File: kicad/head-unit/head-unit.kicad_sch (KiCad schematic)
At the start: 59 parts, among them J1 Debug_Port, J2 Relay_Main_Power, J3 Steering_Wheel, J4 Power Port, J5 Car Connection, J6 Relay_Ign_Detect, J7 Pi, J8 DAC+, K1 Relay_Aux_Power, K2 Relay_Amplifier, SW1 SW_RST, U1 ADP1108AN-3.3, U2 STM32F401RCTx, U3 ADP1108AN-5

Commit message: Dankje Douwe
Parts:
- removed C10: 100uF, Capacitor_SMD:C_1206_3216Metric, symbol Device:C
- removed L2: 20nH, Inductor_SMD:L_0603_1608Metric, symbol Device:L
- removed R5: 100R, Resistor_SMD:R_0402_1005Metric, symbol Device:R
- removed R6: 456K, Resistor_SMD:R_0402_1005Metric, symbol Device:R
- removed R7: 33K, Resistor_SMD:R_0402_1005Metric, symbol Device:R
- removed U3: ADP1108AN-5, Package_DIP:DIP-8_W7.62mm, symbol Regulator_Switching:ADP1108AN-5
- added C12: 100uF, Capacitor_SMD:C_1206_3216Metric, symbol Device:C
- added J9: Amp_Remote, symbol Connector_Generic:Conn_01x01
- R3: value 456K -> 9K
- R4: value 33K -> 3K3
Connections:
- net +5V: now also D2.1 (K), K1.A2
- net Aux_Power: no longer K1.A2
- net GND: now also C12.2
- net +12V_Switched: now reaches J2.87, K1.14, R1.1, U1.2 (Vin), U1.3 (SW1)
- net +12V_Switched: now also C12.1
- net Amp_Remote: no longer names the net of K2.14
- net Amp_Remote: now also J9.1 (Pin_1)
- no-connect marks 66 -> 64
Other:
- added sheet 12 to 5V (12v_to_5v.kicad_sch)
- moved on the sheet: J2, J6

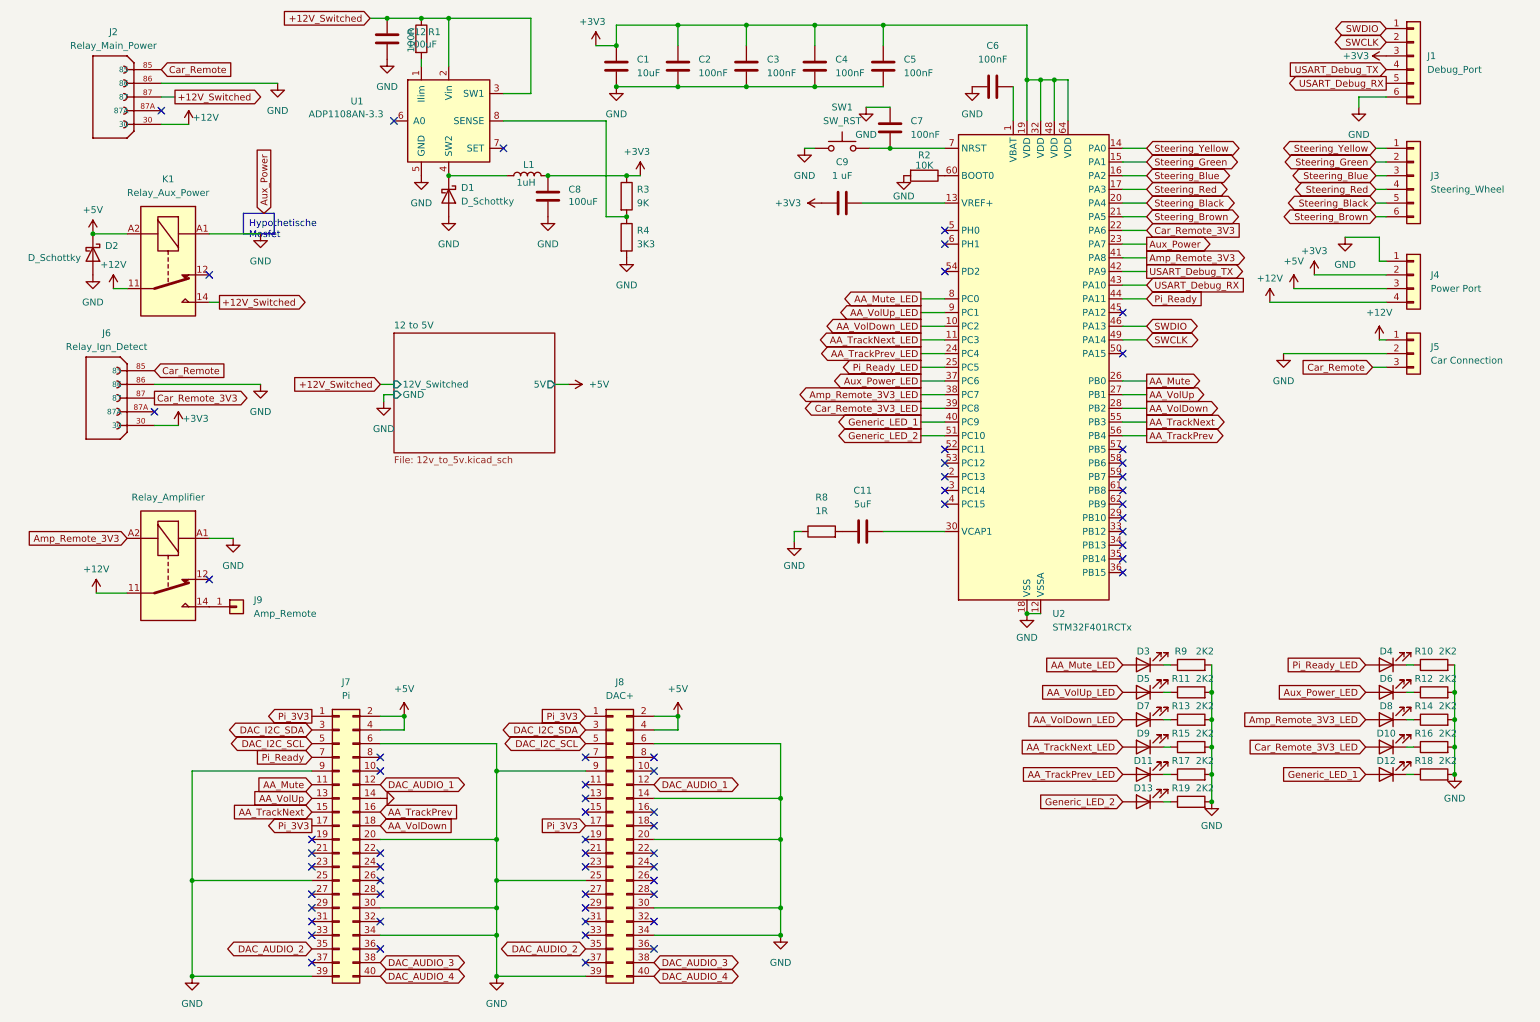
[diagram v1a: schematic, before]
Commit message: Fix mosfets, switch to screw terminals and XT60
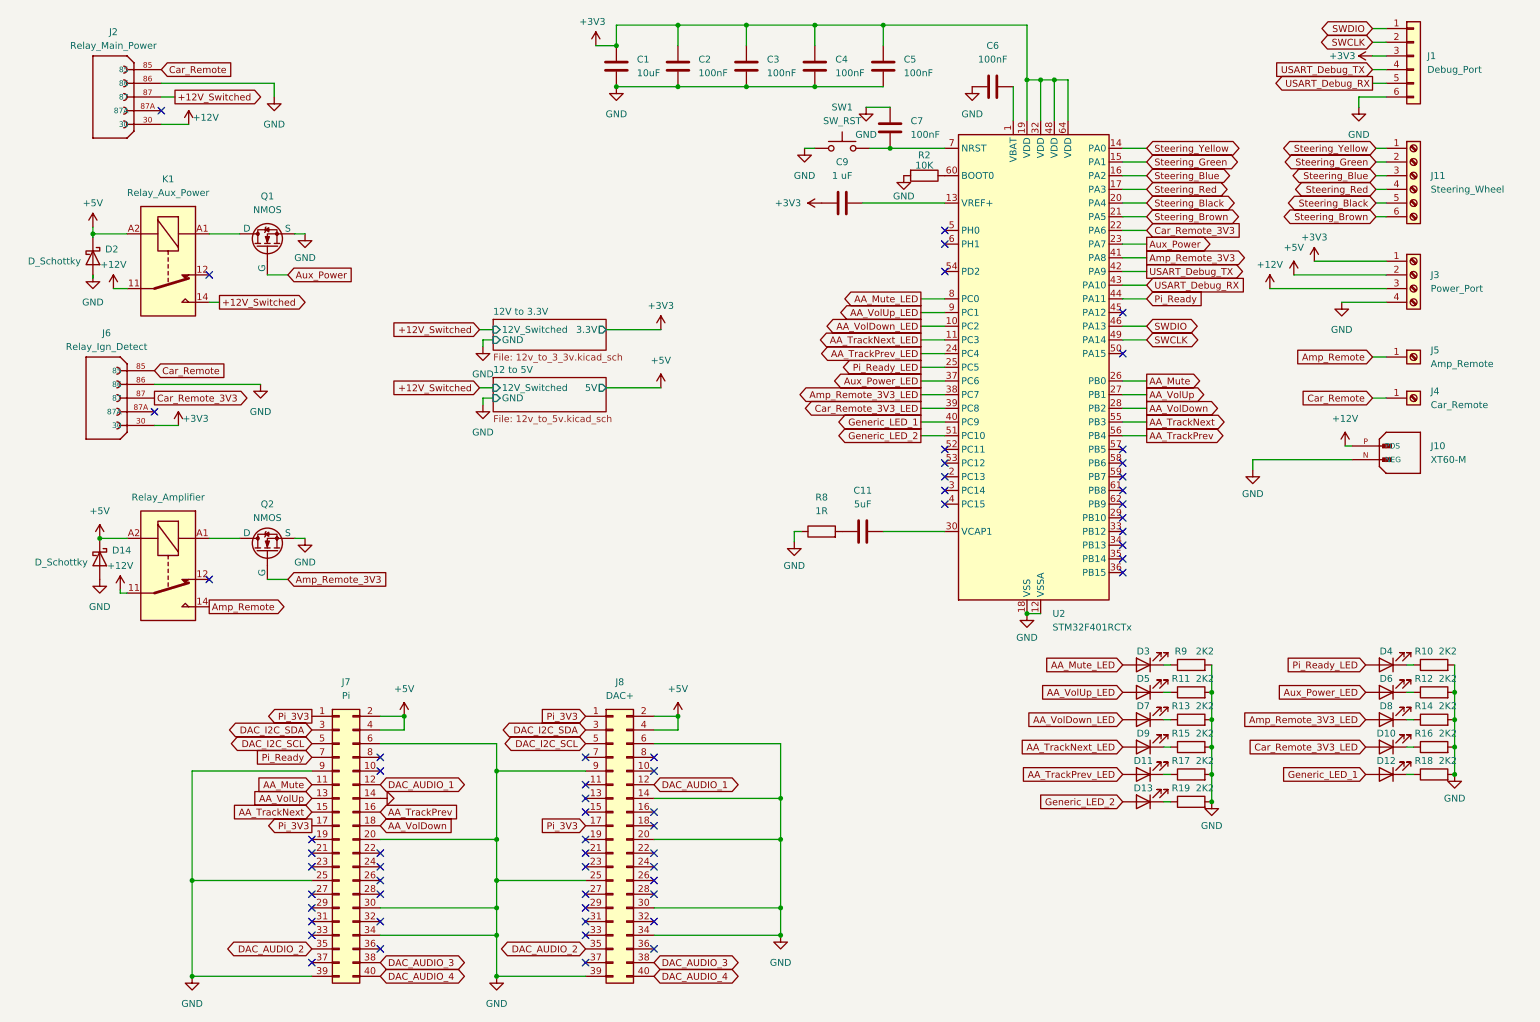
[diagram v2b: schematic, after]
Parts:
- removed C12, C8: 100uF, Capacitor_SMD:C_1206_3216Metric, symbol Device:C
- removed D1: D_Schottky, Diode_SMD:D_0603_1608Metric, symbol Device:D_Schottky
- removed J3: Steering_Wheel, Connector_PinHeader_2.54mm:PinHeader_1x06_P2.54mm_Vertical, symbol Connector_Generic:Conn_01x06
- removed J4: Power Port, Connector_PinHeader_2.54mm:PinHeader_1x04_P2.54mm_Vertical, symbol Connector_Generic:Conn_01x04
- removed J5: Car Connection, Connector_PinHeader_2.54mm:PinHeader_1x03_P2.54mm_Vertical, symbol Connector_Generic:Conn_01x03
- removed J9: Amp_Remote, symbol Connector_Generic:Conn_01x01
- removed L1: 1uH, Inductor_SMD:L_0402_1005Metric, symbol Device:L
- removed R1: 100R, Resistor_SMD:R_0402_1005Metric, symbol Device:R
- removed R3: 9K, Resistor_SMD:R_0402_1005Metric, symbol Device:R
- removed R4: 3K3, Resistor_SMD:R_0402_1005Metric, symbol Device:R
- removed U1: ADP1108AN-3.3, Package_DIP:DIP-8_W7.62mm, symbol Regulator_Switching:ADP1108AN-3.3
- added D14: D_Schottky, Diode_SMD:D_0603_1608Metric, symbol Device:D_Schottky
- added J10: XT60-M, xt60:AMASS_XT60-M, symbol XT60-M:XT60-M
- added J11: Steering_Wheel, TerminalBlock:TerminalBlock_bornier-6_P5.08mm, symbol Connector:Screw_Terminal_01x06
- added J3: Power_Port, TerminalBlock:TerminalBlock_bornier-4_P5.08mm, symbol Connector:Screw_Terminal_01x04
- added J4: Car_Remote, TerminalBlock_MetzConnect:TerminalBlock_MetzConnect_360272_1x01_Horizontal_ScrewM2.6, symbol Connector:Screw_Terminal_01x01
- added J5: Amp_Remote, TerminalBlock_MetzConnect:TerminalBlock_MetzConnect_360272_1x01_Horizontal_ScrewM2.6, symbol Connector:Screw_Terminal_01x01
- added Q1, Q2: NMOS, Button_Switch_SMD:SW_SPDT_CK-JS102011SAQN, symbol Simulation_SPICE:NMOS
- J2, J6: footprint external_symbols:TE_VCF4-1000 -> vcf4:TE_VCF4-1000
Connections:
- net +12V: now also J10.P (POS), J3.3 (Pin_3)
- net +3V3: now also J3.1 (Pin_1)
- net +5V: now also K2.A2, D14.1 (K), J3.2 (Pin_2)
- net Amp_Remote_3V3: now also Q2.2 (G); no longer K2.A2
- net Aux_Power: now also Q1.2 (G)
- net Car_Remote: now also J4.1 (Pin_1)
- net GND: now also D14.2 (A), J10.N (NEG), J3.4 (Pin_4), Q1.3 (S), Q2.3 (S); no longer K1.A1, K2.A1
- net Steering_Black: now also J11.5 (Pin_5)
- net Steering_Blue: now also J11.3 (Pin_3)
- net Steering_Brown: now also J11.6 (Pin_6)
- net Steering_Green: now also J11.2 (Pin_2)
- net Steering_Red: now also J11.4 (Pin_4)
- net Steering_Yellow: now also J11.1 (Pin_1)
- net Amp_Remote: now reaches K2.14
- net Amp_Remote: now also J5.1 (Pin_1)
- new net: K2.A1, Q2.1 (D)
- new net: K1.A1, Q1.1 (D)
- no-connect marks 64 -> 62
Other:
- added sheet 12V to 3.3V (12v_to_3_3v.kicad_sch)
- moved on the sheet: D2

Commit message: Add I2C, begin routing
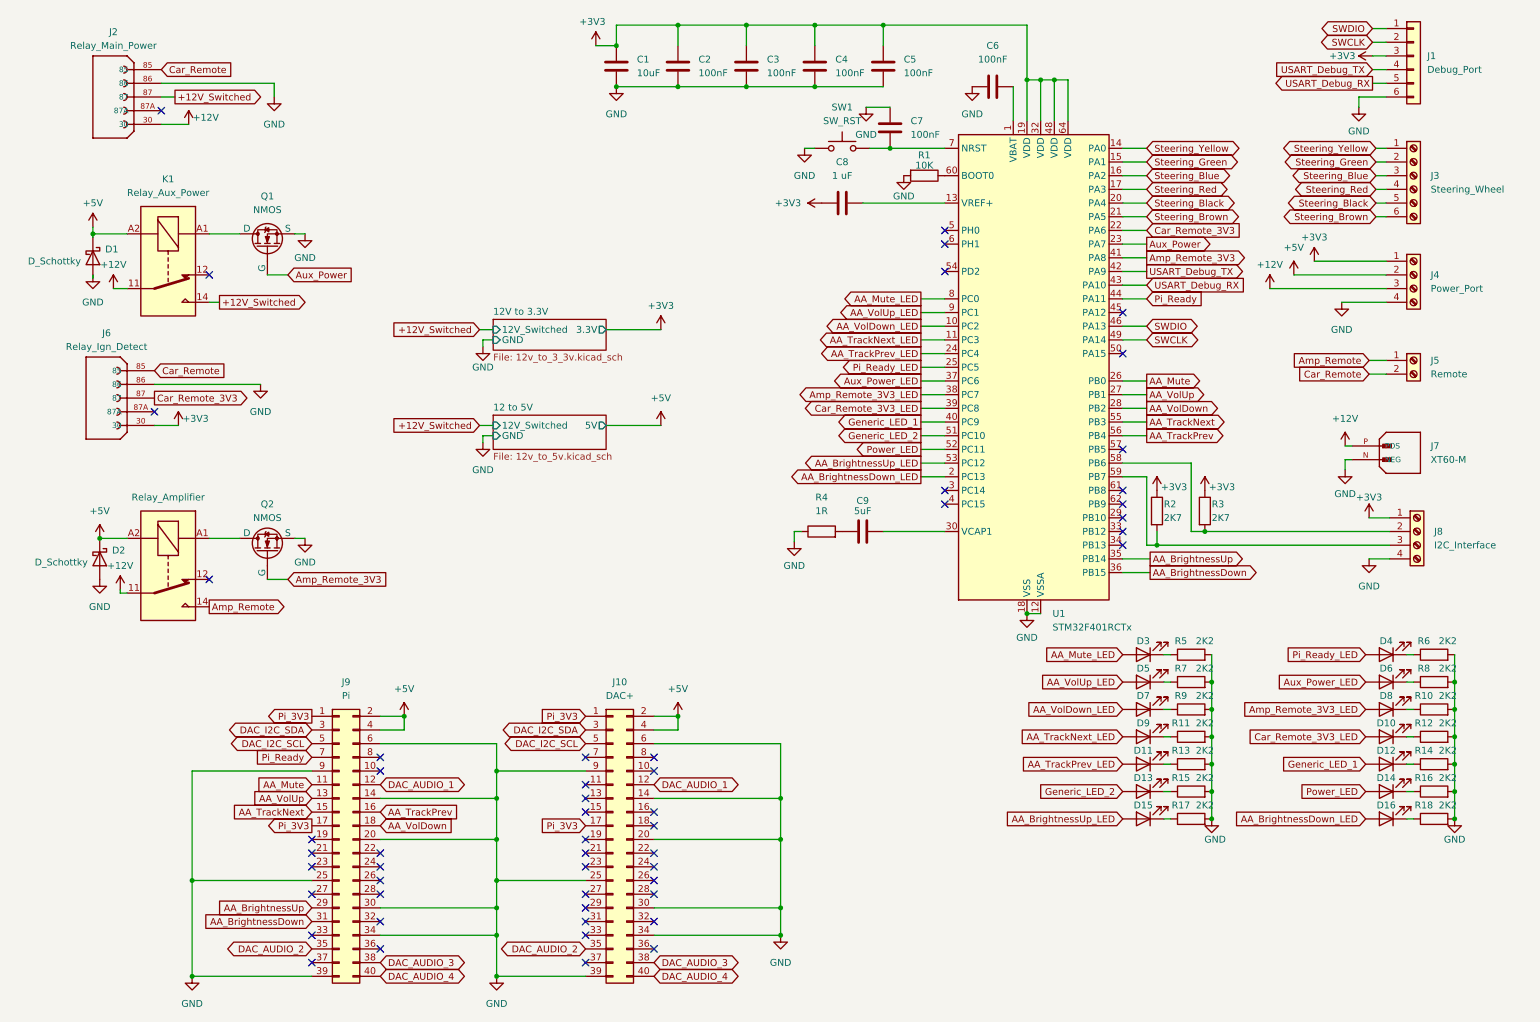
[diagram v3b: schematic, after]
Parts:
- removed J4: Car_Remote, TerminalBlock_MetzConnect:TerminalBlock_MetzConnect_360272_1x01_Horizontal_ScrewM2.6, symbol Connector:Screw_Terminal_01x01
- removed J5: Amp_Remote, TerminalBlock_MetzConnect:TerminalBlock_MetzConnect_360272_1x01_Horizontal_ScrewM2.6, symbol Connector:Screw_Terminal_01x01
- added D14, D15, D16: LED, LED_SMD:LED_0603_1608Metric, symbol Device:LED
- added J5: Remote, TerminalBlock:TerminalBlock_bornier-2_P5.08mm, symbol Connector:Screw_Terminal_01x02
- added J8: I2C_Interface, TerminalBlock:TerminalBlock_bornier-4_P5.08mm, symbol Connector:Screw_Terminal_01x04
- added R16, R17, R18: 2K2, Resistor_SMD:R_0402_1005Metric, symbol Device:R
- added R2, R3: 2K7, Resistor_SMD:R_0402_1005Metric, symbol Device:R
- Q1, Q2: footprint Button_Switch_SMD:SW_SPDT_CK-JS102011SAQN -> Button_Switch_SMD:SW_SPDT_CK_JS102011SAQN
- renumbered C9 to C8, C11 to C9, D2 to D1, D14 to D2, J8 to J10, J11 to J3, J3 to J4, J10 to J7, J7 to J9, R2 to R1, R14 to R10, R15 to R11, R16 to R12, R17 to R13, R18 to R14, R19 to R15, R8 to R4, R9 to R5, R10 to R6, R11 to R7, R12 to R8, R13 to R9, U2 to U1
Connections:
- net +3V3: now also J8.1 (Pin_1), R2.1, R3.1
- net Amp_Remote: now also J5.1 (Pin_1)
- net Car_Remote: now also J5.2 (Pin_2)
- net GND: now also J8.4 (Pin_4), R16.2, R17.2, R18.2
- net AA_BrightnessDown_LED: now reaches U1.2 (PC13)
- net AA_BrightnessDown_LED: now also D16.2 (A)
- net AA_BrightnessUp: now reaches U1.35 (PB14)
- net AA_BrightnessUp: now also J9.29 (Pin_29)
- net AA_BrightnessDown: now reaches U1.36 (PB15)
- net AA_BrightnessDown: now also J9.31 (Pin_31)
- net Power_LED: now reaches U1.52 (PC11)
- net Power_LED: now also D14.2 (A)
- net AA_BrightnessUp_LED: now reaches U1.53 (PC12)
- net AA_BrightnessUp_LED: now also D15.2 (A)
- net at U1.58 (PB6): now also J8.2 (Pin_2), R3.2
- net at U1.59 (PB7): now also J8.3 (Pin_3), R2.2
- new net: D14.1 (K), R16.1
- new net: D16.1 (K), R18.1
- new net: D15.1 (K), R17.1
- no-connect marks 62 -> 53
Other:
- moved on the sheet: D10, D11, D12, D13, D3, D4, D5, D6, D7, D8, D9, R10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

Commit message: WIP routing
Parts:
- Q1, Q2: footprint Button_Switch_SMD:SW_SPDT_CK_JS102011SAQN -> Button_Switch_SMD:SW_SPDT_CK-JS102011SAQN
- R1: footprint Resistor_SMD:R_0402_1005Metric -> Resistor_SMD:R_0603_1608Metric
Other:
- moved on the sheet: J1, J3, J4, J5, J7, Q1, Q2
